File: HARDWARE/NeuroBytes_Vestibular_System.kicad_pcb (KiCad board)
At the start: 2 copper layers, 28 parts, among them P1 JST GH 4-POS, P5 JST GH 4-POS, P6 JST GH 4-POS, P7 JST GH 4-POS, P8 JST GH 7-POS, Q1 NPN_dual, Q2 NPN_dual, SW1 SW_PUSH_TL3330AF130QG, U1 STM32L011Gx, U2 LD3985G33R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

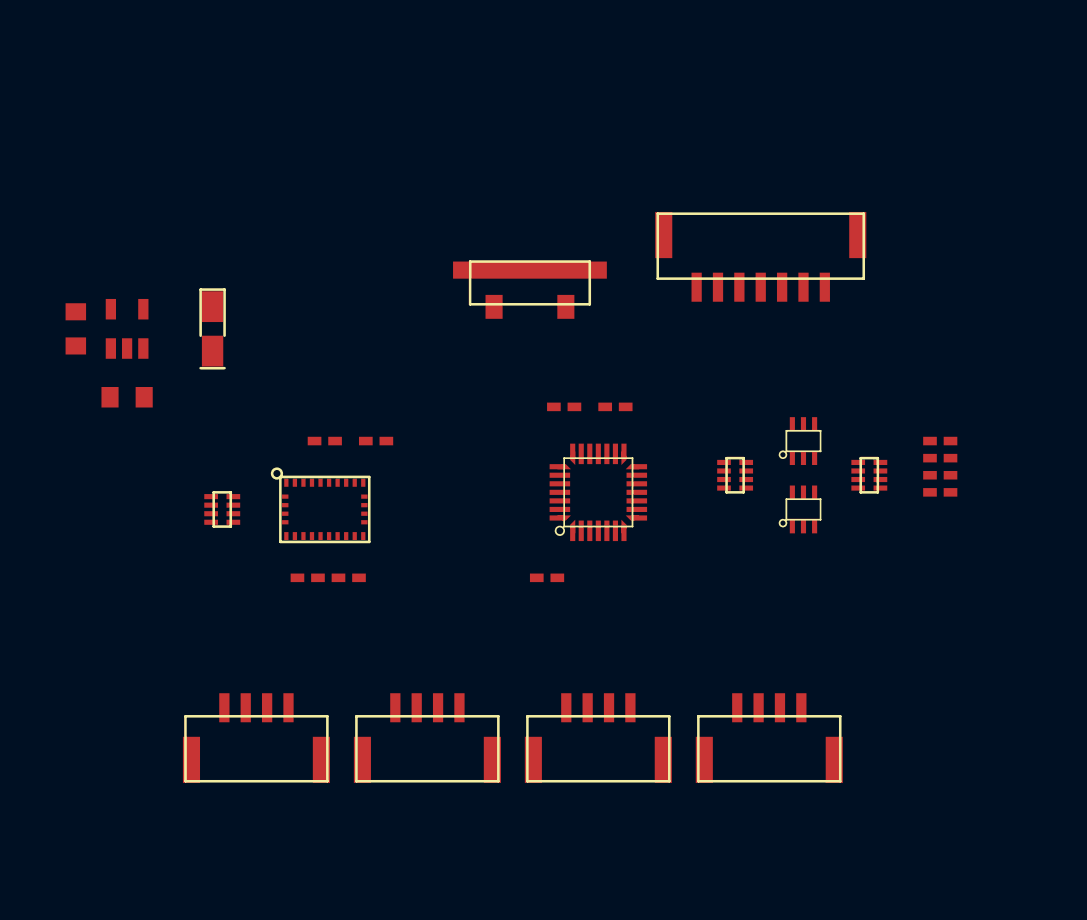
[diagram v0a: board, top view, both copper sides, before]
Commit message: Updated graphics to improve 3D orthoganol canal effect.
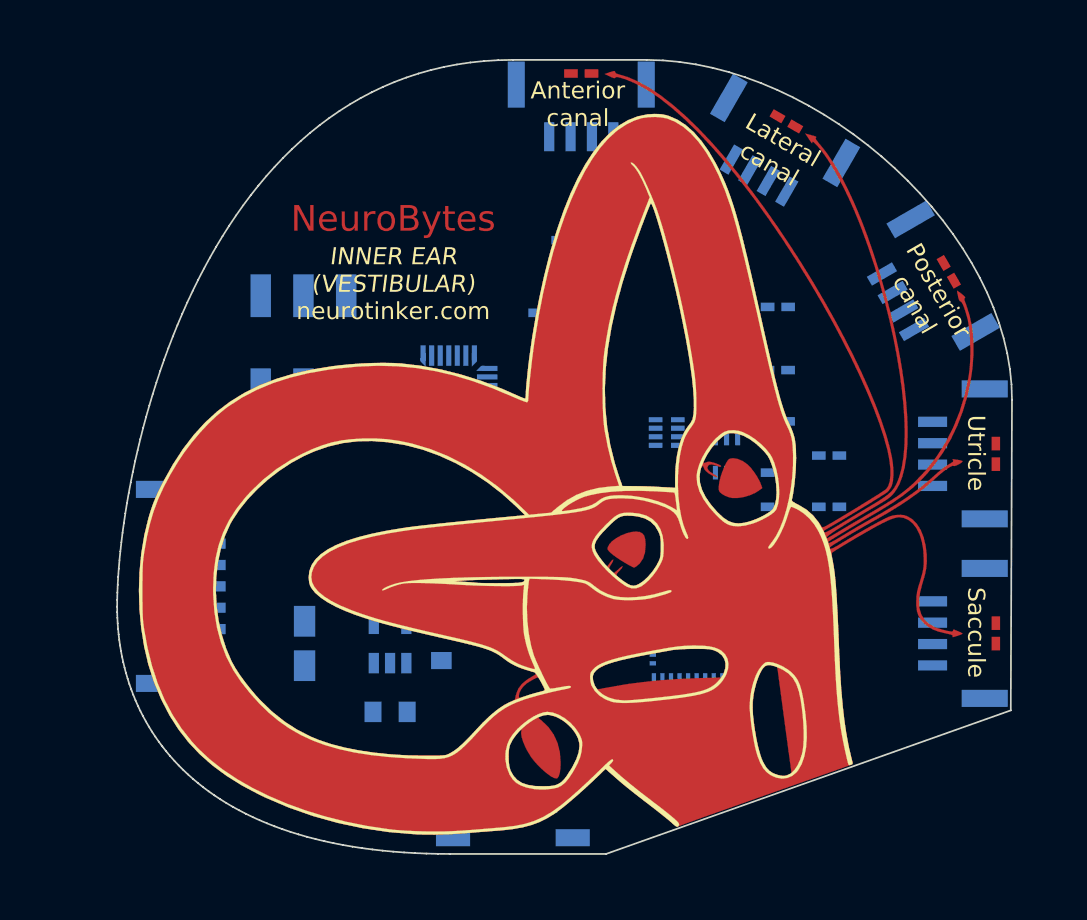
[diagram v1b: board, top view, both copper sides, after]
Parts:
- removed Q1: NPN_dual, KiCad_Footprints:ZF_SMD_SOT-363
- removed RN1: 1k_x4, KiCad_Footprints:ZF_RN_4iso_CTS-0804
- removed RN3: 100_x4, KiCad_Footprints:ZF_RN_4iso_CTS-0804
- added D5: LED, KiCad_Footprints:ZF_SMD_NonPol_0402, F.Cu at (251.2, 92.2)
- added G***: LOGO, KiCad_Footprints:ZF_LOGO_Vestibular_System, F.Cu at (226.6, 81.7)
- added P2: JST GH 4-POS, KiCad_Footprints:ZF_CONN_JST_GH, B.Cu at (227.0, 61.5)
- added R1: R, KiCad_Footprints:ZF_SMD_NonPol_0402, B.Cu at (238.5, 84.8)
- added R2: R, KiCad_Footprints:ZF_SMD_NonPol_0402, B.Cu at (238.5, 79.8)
- added R3: R, KiCad_Footprints:ZF_SMD_NonPol_0402, B.Cu at (241.5, 84.8)
- added R5: R, KiCad_Footprints:ZF_SMD_NonPol_0402, B.Cu at (238.5, 76.8)
- added R6: R, KiCad_Footprints:ZF_SMD_NonPol_0402, B.Cu at (241.5, 81.8)
- added R7: R, KiCad_Footprints:ZF_SMD_NonPol_0402, B.Cu at (238.5, 82.8)
- added R8: R, KiCad_Footprints:ZF_SMD_NonPol_0402, B.Cu at (238.5, 86.8)
- added SW2: Switch_DPDT, KiCad_Footprints:ZF_SW_Slide_DPDT_SMD, B.Cu at (210.8, 75.2)
- C1, C2, C3, C4, C5, C6, C7, C8, C9, P1, P5, P6, P7, P8, Q2, R4, RN2, SW1, U1, U2, U3: moved to B.Cu
- moved P7 47.4 mm to (247.0, 72.0), turned to 30 degrees
- moved P5 40.4 mm to (238.2, 64.0), turned to 60 degrees
- moved P8 39.2 mm to (203.8, 89.5), turned to 180 degrees
- moved SW1 32.5 mm to (223.0, 103.0)
- moved D4 30.1 mm to (227.0, 59.5), turned to 180 degrees
- moved C4 28.2 mm to (218.8, 92.8)
- moved C8 27.6 mm to (238.5, 73.2), turned to 180 degrees
- moved P1 27.4 mm to (249.2, 81.8), turned to 0 degrees
- moved RN2 26.4 mm to (232.0, 80.5), turned to 180 degrees
- moved C7 25.9 mm to (235.8, 96.7), turned to 180 degrees
- moved C1 24.0 mm to (215.8, 96.8), turned to 180 degrees
- moved U2 24.0 mm to (215.8, 92.8), turned to 180 degrees
- moved D3 23.5 mm to (239.0, 62.3), turned to 150 degrees
- moved U3 23.0 mm to (233.5, 93.2), turned to 180 degrees
- moved C9 22.0 mm to (235.5, 73.2), turned to 180 degrees
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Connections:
- D1 pad 1: Net-(D1-Pad1) -> LED_X0
- D1 pad 2: +5V -> Net-(D1-Pad2)
- D2 pad 1: Net-(D2-Pad1) -> LED_X0
- D2 pad 2: +5V -> Net-(D2-Pad2)
- D3 pad 1: Net-(D3-Pad1) -> LED_X1
- D3 pad 2: +5V -> Net-(D3-Pad2)
- D4 pad 1: Net-(D4-Pad1) -> LED_X1
- D4 pad 2: +5V -> Net-(D4-Pad2)
- RN2 pad 7: nRESET -> Net-(RN2-Pad7)
- U1 pad 10: nRESET -> A4IN
- U1 pad 11: INT -> A4EX
- U1 pad 14: Net-(U1-Pad14) -> LED_Y0
- U1 pad 15: Net-(U1-Pad15) -> A2EX
- U1 pad 25: A2EX -> INT
- U1 pad 27: LED_3 -> LED_Y1
- U1 pad 28: LED_2 -> LED_X2
- U1 pad 6: LED_1 -> LED_X1
- U1 pad 7: LED_0 -> LED_X0
- U1 pad 8: A4IN -> A5IN
- U1 pad 9: A4EX -> A5EX
- U3 pad 11: nRESET -> Net-(RN2-Pad7)
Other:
- board outline added: 52.3 x 46.4 mm
- board text added: "Anterior canal"
- board text added: "INNER EAR (VESTIBULAR)"
- board text added: "Lateral canal"
- board text added: "NeuroBytes"
- board text added: "Posterior canal"
- board text added: "Saccule"
- board text added: "Utricle"
- board text added: "neurotinker.com"

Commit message: first PCB routing revision.
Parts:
- removed RN2: 10k_x4, KiCad_Footprints:ZF_RN_4iso_CTS-0804
- removed SW2: Switch_DPDT, KiCad_Footprints:ZF_SW_Slide_DPDT_SMD
- added D10: LED, KiCad_Footprints:ZF_SMD_NonPol_0402, F.Cu at (250.6, 95.6)
- added D11: LED, KiCad_Footprints:ZF_SMD_NonPol_0402, B.Cu at (240.7, 91.8)
- added D12: LED, KiCad_Footprints:ZF_SMD_NonPol_0402, B.Cu at (232.1, 91.8)
- added D6: LED, KiCad_Footprints:ZF_SMD_NonPol_0402, F.Cu at (242.8, 65.0)
- added D7: LED, KiCad_Footprints:ZF_SMD_NonPol_0402, F.Cu at (250.6, 78.5)
- added D8: LED, KiCad_Footprints:ZF_SMD_NonPol_0402, F.Cu at (250.6, 85.0)
- added D9: LED, KiCad_Footprints:ZF_SMD_NonPol_0402, F.Cu at (250.6, 89.0)
- added G***: LOGO, KiCad_Footprints:ZF_LOGO_face, B.Cu at (227.7, 102.6)
- added G***: LOGO, KiCad_Footprints:ZF_LOGO_OSHW, B.Cu at (215.1, 91.9)
- added Q1: NPN_dual, KiCad_Footprints:ZF_SMD_SOT-363, B.Cu at (243.0, 84.3)
- added REF**: ZF_STRUCT_HDR_SMT, KiCad_Footprints:ZF_STRUCT_HDR_SMT, B.Cu at (246.1, 96.8)
- added REF**: ZF_STRUCT_HDR_SMT, KiCad_Footprints:ZF_STRUCT_HDR_SMT, B.Cu at (234.2, 101.0)
- added REF**: ZF_STRUCT_HDR_SMT, KiCad_Footprints:ZF_STRUCT_HDR_SMT, B.Cu at (231.9, 101.9)
- added RN1: 100 x4, KiCad_Footprints:ZF_RN_4iso_CTS-0804, B.Cu at (234.0, 61.2)
- added RN3: 100 x4, KiCad_Footprints:ZF_RN_4iso_CTS-0804, B.Cu at (245.0, 77.4)
- added RN4: 150 x4, KiCad_Footprints:ZF_RN_4iso_CTS-0804, B.Cu at (245.0, 87.0)
- R5, R6, R7, R8: value R -> 10k
- moved C1 34.7 mm to (217.4, 62.2), turned to 90 degrees
- moved D1 34.4 mm to (224.4, 60.2)
- moved D5 34.1 mm to (236.7, 61.4), turned to 60 degrees
- moved U2 31.0 mm to (220.4, 62.2), turned to 90 degrees
- moved C5 30.2 mm to (207.1, 92.6), turned to 270 degrees
- moved C4 28.3 mm to (220.5, 64.6), turned to 180 degrees
- moved D4 27.3 mm to (249.8, 74.5), turned to 30 degrees
- moved C2 18.3 mm to (223.8, 80.0), turned to 0 degrees
- moved R6 18.1 mm to (224.9, 89.0), turned to 180 degrees
- moved R8 16.5 mm to (222.1, 85.3), turned to 180 degrees
- moved R4 14.3 mm to (213.3, 73.7), turned to 270 degrees
- moved R5 14.0 mm to (230.4, 88.3), turned to 90 degrees
- moved R7 14.0 mm to (224.5, 82.1), turned to 90 degrees
- moved C8 14.0 mm to (227.8, 82.2), turned to 0 degrees
- moved C9 12.7 mm to (227.8, 83.2), turned to 0 degrees
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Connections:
- D2 pad 1: LED_X0 -> LED_X3
- D4 pad 1: LED_X1 -> LED_X2
- P8 pad 6: MOSI -> IDENTIFY
- R1 pad 2: LED_Y0 -> LED_Y1
- R2 pad 2: LED_Y1 -> LED_Y2
- R3 pad 1: Net-(Q2-Pad6) -> Net-(Q1-Pad2)
- R3 pad 2: Net-(D1-Pad2) -> LED_Y0
- R5 pad 1: Net-(Q2-Pad6) -> Net-(R5-Pad1)
- R5 pad 2: Net-(D3-Pad2) -> +3V3
- R6 pad 1: Net-(Q2-Pad6) -> Net-(R6-Pad1)
- R6 pad 2: Net-(D5-Pad2) -> +3V3
- R7 pad 1: Net-(Q2-Pad3) -> SDA
- R7 pad 2: Net-(D2-Pad2) -> +3V3
- R8 pad 1: Net-(Q2-Pad3) -> SCL
- R8 pad 2: Net-(D4-Pad2) -> +3V3
- U1 pad 10: A4IN -> LED_Y2
- U1 pad 11: A4EX -> A2IN
- U1 pad 12: A2IN -> A2EX
- U1 pad 13: A3IN -> A4IN
- U1 pad 15: A2EX -> A4EX
- U1 pad 18: A1EX -> LED_X0
- U1 pad 2: A3EX -> A5IN
- U1 pad 24: IDENTIFY -> A1IN
- U1 pad 25: INT -> A1EX
- U1 pad 26: MOSI -> IDENTIFY
- U1 pad 27: LED_Y1 -> LED_X3
- U1 pad 28: LED_X2 -> LED_X1
- U1 pad 3: A1IN -> A5EX
- U1 pad 6: LED_X1 -> A3IN
- U1 pad 7: LED_X0 -> LED_X2
- U1 pad 8: A5IN -> A3EX
- U1 pad 9: A5EX -> LED_Y1
- U3 pad 10: GND -> Net-(U3-Pad10)
- U3 pad 11: Net-(RN2-Pad7) -> Net-(R6-Pad1)
- U3 pad 14: INT -> Net-(U3-Pad14)
- U3 pad 4: Net-(RN2-Pad8) -> Net-(R5-Pad1)
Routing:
- net GND: track 0.00 -> 164.2 mm, vias 0 -> 31
- net +5V: track 0.00 -> 111.4 mm, vias 0 -> 11
- net LED_X1: track 0.00 -> 101.5 mm, vias 0 -> 7
- net LED_X3: track 0.00 -> 83.7 mm, vias 0 -> 7
- net LED_X2: track 0.00 -> 80.2 mm, vias 0 -> 8
- net LED_X0: track 0.00 -> 70.7 mm, vias 0 -> 7
- net +3V3: track 0.00 -> 58.7 mm, vias 0 -> 2
- net A1EX: track 0.00 -> 52.3 mm, vias 0 -> 2
- net A1IN: track 0.00 -> 51.4 mm, vias 0 -> 2
- net IDENTIFY: track 0.00 -> 45.3 mm, vias 0 -> 2
- net A4EX: track 0.00 -> 34.8 mm, vias 0 -> 2
- net A4IN: track 0.00 -> 34.7 mm
- net RESET: track 0.00 -> 33.6 mm, vias 0 -> 2
- net A5IN: track 0.00 -> 30.4 mm, vias 0 -> 2
- net A2EX: track 0.00 -> 28.1 mm
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- added copper zone on B.Cu, net GND
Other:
- board text added: "HOLD TO CHANGE"
- board text added: "ID"
- board text added: "LEFT"
- board text added: "RIGHT"
- board text added: "VESTIBULAR SYSTEM"
- board text added: "®"
- board text removed: "INNER EAR (VESTIBULAR)"
